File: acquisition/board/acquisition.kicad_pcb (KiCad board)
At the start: 4 copper layers, 0 parts

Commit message: Finished footprint assignment
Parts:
- added C1: 0.1 uF, azonenberg_pcb:EIA_0402_CAP_NOSILK, F.Cu at (151.9, 72.8)
- added C10: 0.1 uF, azonenberg_pcb:EIA_0402_CAP_NOSILK, F.Cu at (141.8, 83.6)
- added C100: 0.47 uF, azonenberg_pcb:EIA_0402_CAP_NOSILK, F.Cu at (151.1, 74.3)
- added C101: 0.47 uF, azonenberg_pcb:EIA_0402_CAP_NOSILK, F.Cu at (141.8, 86.6)
- added C102: 0.47 uF, azonenberg_pcb:EIA_0402_CAP_NOSILK, F.Cu at (113.7, 113.7)
- added C103: 0.47 uF, azonenberg_pcb:EIA_0402_CAP_NOSILK, F.Cu at (111.2, 112.2)
- added C104: 0.47 uF, azonenberg_pcb:EIA_0402_CAP_NOSILK, F.Cu at (139.3, 86.8)
- added C105: 0.47 uF, azonenberg_pcb:EIA_0402_CAP_NOSILK, F.Cu at (146.8, 85.1)
- added C106: 0.47 uF, azonenberg_pcb:EIA_0402_CAP_NOSILK, F.Cu at (139.3, 85.3)
- added C107: 0.47 uF, azonenberg_pcb:EIA_0402_CAP_NOSILK, F.Cu at (149.4, 72.8)
- added C108: 4.7 uF, azonenberg_pcb:EIA_0603_CAP_NOSILK, F.Cu at (66.0, 54.9)
- added C109: 4.7 uF, azonenberg_pcb:EIA_0603_CAP_NOSILK, F.Cu at (55.4, 49.4)
- added C11: 0.1 uF, azonenberg_pcb:EIA_0402_CAP_NOSILK, F.Cu at (148.6, 76.1)
- added C110: 4.7 uF, azonenberg_pcb:EIA_0603_CAP_NOSILK, F.Cu at (58.7, 51.2)
- added C111: 4.7 uF, azonenberg_pcb:EIA_0603_CAP_NOSILK, F.Cu at (55.4, 51.2)
- added C112: 0.47 uF, azonenberg_pcb:EIA_0402_CAP_NOSILK, F.Cu at (65.6, 64.0)
- added C113: 0.47 uF, azonenberg_pcb:EIA_0402_CAP_NOSILK, F.Cu at (65.6, 59.5)
- added C114: 0.47 uF, azonenberg_pcb:EIA_0402_CAP_NOSILK, F.Cu at (78.1, 60.7)
- added C115: 0.47 uF, azonenberg_pcb:EIA_0402_CAP_NOSILK, F.Cu at (65.6, 58.0)
- added C116: 0.47 uF, azonenberg_pcb:EIA_0402_CAP_NOSILK, F.Cu at (92.0, 45.6)
- added C117: 0.47 uF, azonenberg_pcb:EIA_0402_CAP_NOSILK, F.Cu at (73.1, 57.7)
- added C118: 0.47 uF, azonenberg_pcb:EIA_0402_CAP_NOSILK, F.Cu at (87.0, 47.1)
- added C119: 0.47 uF, azonenberg_pcb:EIA_0402_CAP_NOSILK, F.Cu at (49.5, 75.9)
- added C12: 0.1 uF, azonenberg_pcb:EIA_0402_CAP_NOSILK, F.Cu at (144.3, 83.6)
- added C120: 0.47 uF, azonenberg_pcb:EIA_0402_CAP_NOSILK, F.Cu at (44.5, 73.5)
- added C121: 0.47 uF, azonenberg_pcb:EIA_0402_CAP_NOSILK, F.Cu at (89.5, 44.1)
- added C122: 0.47 uF, azonenberg_pcb:EIA_0402_CAP_NOSILK, F.Cu at (47.0, 72.0)
- added C123: 0.47 uF, azonenberg_pcb:EIA_0402_CAP_NOSILK, F.Cu at (68.1, 56.5)
- added C124: 0.47 uF, azonenberg_pcb:EIA_0402_CAP_NOSILK, F.Cu at (49.5, 72.9)
- added C125: 0.47 uF, azonenberg_pcb:EIA_0402_CAP_NOSILK, F.Cu at (80.6, 56.2)
- added C126: 0.47 uF, azonenberg_pcb:EIA_0402_CAP_NOSILK, F.Cu at (87.0, 44.1)
- added C127: 0.47 uF, azonenberg_pcb:EIA_0402_CAP_NOSILK, F.Cu at (44.5, 75.0)
- added C128: 4.7 uF, azonenberg_pcb:EIA_0603_CAP_NOSILK, F.Cu at (48.2, 70.3)
- added C129: 4.7 uF, azonenberg_pcb:EIA_0603_CAP_NOSILK, F.Cu at (58.7, 49.4)
- added C13: 0.47 uF, azonenberg_pcb:EIA_0402_CAP_NOSILK, F.Cu at (145.4, 79.1)
- added C130: 4.7 uF, azonenberg_pcb:EIA_0603_CAP_NOSILK, F.Cu at (48.2, 68.5)
- added C131: 4.7 uF, azonenberg_pcb:EIA_0603_CAP_NOSILK, F.Cu at (44.9, 68.5)
- added C132: 0.47 uF, azonenberg_pcb:EIA_0402_CAP_NOSILK, F.Cu at (78.1, 56.2)
- added C133: 0.47 uF, azonenberg_pcb:EIA_0402_CAP_NOSILK, F.Cu at (75.6, 60.7)
- added C134: 0.47 uF, azonenberg_pcb:EIA_0402_CAP_NOSILK, F.Cu at (59.5, 76.0)
- added C135: 0.47 uF, azonenberg_pcb:EIA_0402_CAP_NOSILK, F.Cu at (73.1, 56.2)
- added C136: 0.47 uF, azonenberg_pcb:EIA_0402_CAP_NOSILK, F.Cu at (73.1, 65.2)
- added C137: 0.47 uF, azonenberg_pcb:EIA_0402_CAP_NOSILK, F.Cu at (70.6, 61.0)
- added C138: 0.47 uF, azonenberg_pcb:EIA_0402_CAP_NOSILK, F.Cu at (57.0, 76.0)
- added C139: 0.47 uF, azonenberg_pcb:EIA_0402_CAP_NOSILK, F.Cu at (68.1, 59.5)
- added C14: 4.7 uF, azonenberg_pcb:EIA_0603_CAP_NOSILK, F.Cu at (129.1, 88.8)
- added C140: 0.47 uF, azonenberg_pcb:EIA_0402_CAP_NOSILK, F.Cu at (44.5, 72.0)
- added C141: 0.47 uF, azonenberg_pcb:EIA_0402_CAP_NOSILK, F.Cu at (44.5, 76.5)
- added C142: 0.47 uF, azonenberg_pcb:EIA_0402_CAP_NOSILK, F.Cu at (75.6, 57.7)
- added C143: 0.47 uF, azonenberg_pcb:EIA_0402_CAP_NOSILK, F.Cu at (68.1, 70.0)
- added C144: 0.47 uF, azonenberg_pcb:EIA_0402_CAP_NOSILK, F.Cu at (68.1, 62.5)
- added C145: 0.47 uF, azonenberg_pcb:EIA_0402_CAP_NOSILK, F.Cu at (75.6, 59.2)
- added C146: 0.47 uF, azonenberg_pcb:EIA_0402_CAP_NOSILK, F.Cu at (87.0, 45.6)
- added C147: 0.47 uF, azonenberg_pcb:EIA_0402_CAP_NOSILK, F.Cu at (89.5, 48.6)
- added C148: 0.47 uF, azonenberg_pcb:EIA_0402_CAP_NOSILK, F.Cu at (72.2, 54.7)
- added C149: 0.47 uF, azonenberg_pcb:EIA_0402_CAP_NOSILK, F.Cu at (84.5, 44.1)
- added C15: 0.47 uF, azonenberg_pcb:EIA_0402_CAP_NOSILK, F.Cu at (151.1, 75.8)
- added C150: 0.47 uF, azonenberg_pcb:EIA_0402_CAP_NOSILK, F.Cu at (80.6, 57.7)
- added C151: 0.47 uF, azonenberg_pcb:EIA_0402_CAP_NOSILK, F.Cu at (73.1, 62.2)
- added C152: 0.47 uF, azonenberg_pcb:EIA_0402_CAP_NOSILK, F.Cu at (82.2, 54.7)
- added C153: 0.47 uF, azonenberg_pcb:EIA_0402_CAP_NOSILK, F.Cu at (78.1, 59.2)
- added C154: 0.47 uF, azonenberg_pcb:EIA_0402_CAP_NOSILK, F.Cu at (47.0, 76.5)
- added C155: 0.47 uF, azonenberg_pcb:EIA_0402_CAP_NOSILK, F.Cu at (52.0, 74.4)
- added C156: 0.47 uF, azonenberg_pcb:EIA_0402_CAP_NOSILK, F.Cu at (87.0, 48.6)
- added C157: 0.47 uF, azonenberg_pcb:EIA_0402_CAP_NOSILK, F.Cu at (68.1, 67.0)
- added C158: 0.47 uF, azonenberg_pcb:EIA_0402_CAP_NOSILK, F.Cu at (70.6, 64.0)
- added C159: 0.47 uF, azonenberg_pcb:EIA_0402_CAP_NOSILK, F.Cu at (73.1, 59.2)
- added C16: 0.47 uF, azonenberg_pcb:EIA_0402_CAP_NOSILK, F.Cu at (142.9, 77.6)
- added C160: 0.47 uF, azonenberg_pcb:EIA_0402_CAP_NOSILK, F.Cu at (54.5, 76.0)
- added C161: 0.47 uF, azonenberg_pcb:EIA_0402_CAP_NOSILK, F.Cu at (89.5, 47.1)
- added C162: 0.47 uF, azonenberg_pcb:EIA_0402_CAP_NOSILK, F.Cu at (84.5, 48.6)
- added C163: 0.47 uF, azonenberg_pcb:EIA_0402_CAP_NOSILK, F.Cu at (89.5, 45.6)
- added C164: 4.7 uF, azonenberg_pcb:EIA_0603_CAP_NOSILK, F.Cu at (110.9, 105.4)
- added C165: 0.1 uF, azonenberg_pcb:EIA_0402_CAP_NOSILK, F.Cu at (111.0, 118.2)
- added C166: 10 nF, azonenberg_pcb:EIA_0603_CAP_NOSILK, F.Cu at (110.9, 103.6)
- added C167: 0.47 uF, azonenberg_pcb:EIA_0402_CAP_NOSILK, F.Cu at (99.1, 119.7)
- added C168: 0.47 uF, azonenberg_pcb:EIA_0402_CAP_NOSILK, F.Cu at (107.9, 115.2)
- added C169: 10 nF, azonenberg_pcb:EIA_0603_CAP_NOSILK, F.Cu at (114.2, 105.4)
- added C17: 0.47 uF, azonenberg_pcb:EIA_0402_CAP_NOSILK, F.Cu at (153.6, 75.8)
- added C170: 4.7 uF, azonenberg_pcb:EIA_0603_CAP_NOSILK, F.Cu at (100.0, 118.0)
- added C171: 4.7 uF, azonenberg_pcb:EIA_0603_CAP_NOSILK, F.Cu at (110.9, 107.2)
- added C172: 0.47 uF, azonenberg_pcb:EIA_0402_CAP_NOSILK, F.Cu at (110.4, 115.2)
- added C173: 0.47 uF, azonenberg_pcb:EIA_0402_CAP_NOSILK, F.Cu at (117.1, 103.5)
- added C174: 0.47 uF, azonenberg_pcb:EIA_0402_CAP_NOSILK, F.Cu at (106.0, 117.8)
- added C175: 0.47 uF, azonenberg_pcb:EIA_0402_CAP_NOSILK, F.Cu at (116.3, 107.0)
- added C176: 0.47 uF, azonenberg_pcb:EIA_0402_CAP_NOSILK, F.Cu at (108.5, 119.8)
- added C177: 0.47 uF, azonenberg_pcb:EIA_0402_CAP_NOSILK, F.Cu at (113.8, 108.5)
- added C178: 0.1 uF, azonenberg_pcb:EIA_0402_CAP_NOSILK, F.Cu at (108.5, 116.8)
- added C179: 0.47 uF, azonenberg_pcb:EIA_0402_CAP_NOSILK, F.Cu at (111.2, 113.7)
- added C18: 0.47 uF, azonenberg_pcb:EIA_0402_CAP_NOSILK, F.Cu at (148.6, 74.6)
- added C180: 4.7 uF, azonenberg_pcb:EIA_0603_CAP_NOSILK, F.Cu at (171.0, 49.4)
- added C181: 0.47 uF, azonenberg_pcb:EIA_0402_CAP_NOSILK, F.Cu at (161.9, 60.0)
- added C182: 0.1 uF, azonenberg_pcb:EIA_0402_CAP_NOSILK, F.Cu at (171.5, 52.5)
- added C183: 0.47 uF, azonenberg_pcb:EIA_0402_CAP_NOSILK, F.Cu at (166.5, 52.5)
- added C184: 0.47 uF, azonenberg_pcb:EIA_0402_CAP_NOSILK, F.Cu at (165.6, 58.5)
- added C185: 0.47 uF, azonenberg_pcb:EIA_0402_CAP_NOSILK, F.Cu at (166.9, 55.5)
- added C186: 0.47 uF, azonenberg_pcb:EIA_0402_CAP_NOSILK, F.Cu at (165.6, 57.0)
- added C187: 0.47 uF, azonenberg_pcb:EIA_0402_CAP_NOSILK, F.Cu at (173.9, 49.2)
- added C188: 0.47 uF, azonenberg_pcb:EIA_0402_CAP_NOSILK, F.Cu at (169.0, 52.5)
- added C189: 0.1 uF, azonenberg_pcb:EIA_0402_CAP_NOSILK, F.Cu at (65.6, 68.5)
- added C19: 4.7 uF, azonenberg_pcb:EIA_0603_CAP_NOSILK, F.Cu at (146.5, 73.0)
- added C190: 0.1 uF, azonenberg_pcb:EIA_0402_CAP_NOSILK, F.Cu at (68.1, 58.0)
- added C191: 0.1 uF, azonenberg_pcb:EIA_0402_CAP_NOSILK, F.Cu at (74.7, 54.7)
- added C192: 0.1 uF, azonenberg_pcb:EIA_0402_CAP_NOSILK, F.Cu at (52.0, 76.0)
- added C193: 10 uF, azonenberg_pcb:EIA_1206_CAP_NOSILK, F.Cu at (75.9, 81.9)
- added C194: 47 uF, azonenberg_pcb:EIA_1206_CAP_NOSILK, F.Cu at (75.9, 84.5)
- added C195: 47 uF, azonenberg_pcb:EIA_1206_CAP_NOSILK, F.Cu at (51.8, 93.5)
- added C196: 47 uF, azonenberg_pcb:EIA_1206_CAP_NOSILK, F.Cu at (55.5, 104.0)
- added C197: 47 uF, azonenberg_pcb:EIA_1206_CAP_NOSILK, F.Cu at (55.5, 101.4)
- added C198: 22 uF, azonenberg_pcb:EIA_1210_CAP_NOSILK, F.Cu at (70.2, 87.9)
- added C199: 22 uF, azonenberg_pcb:EIA_1210_CAP_NOSILK, F.Cu at (75.2, 87.9)
- added C2: 0.1 uF, azonenberg_pcb:EIA_0402_CAP_NOSILK, F.Cu at (147.6, 82.1)
- added C20: 0.47 uF, azonenberg_pcb:EIA_0402_CAP_NOSILK, F.Cu at (150.1, 80.6)
- added C200: 22 uF, azonenberg_pcb:EIA_1210_CAP_NOSILK, F.Cu at (61.2, 97.7)
- added C201: 22 uF, azonenberg_pcb:EIA_1210_CAP_NOSILK, F.Cu at (68.6, 92.3)
- added C202: 1 uF, azonenberg_pcb:EIA_0603_CAP_NOSILK, F.Cu at (69.3, 54.9)
- added C203: 1 uF, azonenberg_pcb:EIA_0603_CAP_NOSILK, F.Cu at (55.4, 53.0)
- added C204: 1 uF, azonenberg_pcb:EIA_0603_CAP_NOSILK, F.Cu at (58.7, 53.0)
- added C205: 1 uF, azonenberg_pcb:EIA_0603_CAP_NOSILK, F.Cu at (44.9, 70.3)
- added C206: 0.1 uF, azonenberg_pcb:EIA_0402_CAP_NOSILK, F.Cu at (79.7, 54.7)
- added C207: 0.1 uF, azonenberg_pcb:EIA_0402_CAP_NOSILK, F.Cu at (70.6, 58.0)
- added C208: 0.1 uF, azonenberg_pcb:EIA_0402_CAP_NOSILK, F.Cu at (62.0, 76.0)
- added C209: 0.1 uF, azonenberg_pcb:EIA_0402_CAP_NOSILK, F.Cu at (78.1, 57.7)
- added C21: 0.47 uF, azonenberg_pcb:EIA_0402_CAP_NOSILK, F.Cu at (139.4, 88.3)
- added C210: DNP, azonenberg_pcb:EIA_0402_CAP_NOSILK, F.Cu at (85.7, 82.8)
- added C211: DNP, azonenberg_pcb:EIA_0402_CAP_NOSILK, F.Cu at (83.2, 82.8)
- added C212: DNP, azonenberg_pcb:EIA_0402_CAP_NOSILK, F.Cu at (61.7, 105.2)
- added C213: DNP, azonenberg_pcb:EIA_0402_CAP_NOSILK, F.Cu at (68.2, 95.0)
- added C214: 4.7 uF, azonenberg_pcb:EIA_0603_CAP_NOSILK, F.Cu at (65.3, 96.6)
- added C215: 4.7 uF, azonenberg_pcb:EIA_0603_CAP_NOSILK, F.Cu at (65.3, 98.4)
- added C216: DNP, azonenberg_pcb:EIA_0402_CAP_NOSILK, F.Cu at (75.7, 90.6)
- added C217: DNP, azonenberg_pcb:EIA_0402_CAP_NOSILK, F.Cu at (70.7, 96.5)
- added C218: 4.7 uF, azonenberg_pcb:EIA_0603_CAP_NOSILK, F.Cu at (79.4, 86.7)
- added C219: 4.7 uF, azonenberg_pcb:EIA_0603_CAP_NOSILK, F.Cu at (72.8, 90.8)
- added C22: 0.47 uF, azonenberg_pcb:EIA_0402_CAP_NOSILK, F.Cu at (141.8, 85.1)
- added C220: 4.7 uF, azonenberg_pcb:EIA_0603_CAP_NOSILK, F.Cu at (110.9, 109.0)
- added C221: 4.7 uF, azonenberg_pcb:EIA_0603_CAP_NOSILK, F.Cu at (65.3, 100.2)
- added C222: 4.7 uF, azonenberg_pcb:EIA_0603_CAP_NOSILK, F.Cu at (72.8, 92.5)
- added C23: 0.47 uF, azonenberg_pcb:EIA_0402_CAP_NOSILK, F.Cu at (139.3, 82.3)
- added C24: 0.47 uF, azonenberg_pcb:EIA_0402_CAP_NOSILK, F.Cu at (131.9, 88.6)
- added C25: 0.47 uF, azonenberg_pcb:EIA_0402_CAP_NOSILK, F.Cu at (147.9, 77.6)
- added C26: 0.47 uF, azonenberg_pcb:EIA_0402_CAP_NOSILK, F.Cu at (153.6, 74.3)
- added C27: 0.47 uF, azonenberg_pcb:EIA_0402_CAP_NOSILK, F.Cu at (152.9, 77.3)
- added C28: 0.47 uF, azonenberg_pcb:EIA_0402_CAP_NOSILK, F.Cu at (139.3, 83.8)
- added C29: 10 uF, azonenberg_pcb:EIA_0805_CAP_NOSILK, F.Cu at (139.8, 78.5)
- added C3: 0.1 uF, azonenberg_pcb:EIA_0402_CAP_NOSILK, F.Cu at (145.1, 80.6)
- added C30: 47 pF, azonenberg_pcb:EIA_0402_CAP_NOSILK, F.Cu at (136.9, 88.6)
- added C31: 3900 pF, azonenberg_pcb:EIA_0402_CAP_NOSILK, F.Cu at (150.4, 77.6)
- added C32: 0.1 uF, azonenberg_pcb:EIA_0402_CAP_NOSILK, F.Cu at (142.6, 82.1)
- added C33: 4.7 uF, azonenberg_pcb:EIA_0603_CAP_NOSILK, F.Cu at (113.7, 84.1)
- added C34: 4.7 uF, azonenberg_pcb:EIA_0603_CAP_NOSILK, F.Cu at (95.4, 95.3)
- added C35: 4.7 uF, azonenberg_pcb:EIA_0603_CAP_NOSILK, F.Cu at (102.1, 88.8)
- added C36: 0.47 uF, azonenberg_pcb:EIA_0402_CAP_NOSILK, F.Cu at (109.1, 95.0)
- added C37: 0.47 uF, azonenberg_pcb:EIA_0402_CAP_NOSILK, F.Cu at (106.6, 93.8)
- added C38: 0.47 uF, azonenberg_pcb:EIA_0402_CAP_NOSILK, F.Cu at (108.3, 90.5)
- added C39: 0.47 uF, azonenberg_pcb:EIA_0402_CAP_NOSILK, F.Cu at (103.3, 92.2)
- added C4: 0.1 uF, azonenberg_pcb:EIA_0402_CAP_NOSILK, F.Cu at (152.9, 78.8)
- added C40: 0.47 uF, azonenberg_pcb:EIA_0402_CAP_NOSILK, F.Cu at (101.6, 95.8)
- added C41: 330 uF, azonenberg_pcb:EIA_1210_CAP_NOSILK, F.Cu at (92.9, 92.4)
- added C42: 100 uF, azonenberg_pcb:EIA_1206_CAP_NOSILK, F.Cu at (92.9, 89.2)
- added C43: 0.47 uF, azonenberg_pcb:EIA_0402_CAP_NOSILK, F.Cu at (104.1, 96.8)
- added C44: 0.47 uF, azonenberg_pcb:EIA_0402_CAP_NOSILK, F.Cu at (110.8, 90.5)
- added C45: 4.7 uF, azonenberg_pcb:EIA_0603_CAP_NOSILK, F.Cu at (100.4, 92.7)
- added C46: 100 uF, azonenberg_pcb:EIA_1206_CAP_NOSILK, F.Cu at (111.2, 81.9)
- added C47: 0.47 uF, azonenberg_pcb:EIA_0402_CAP_NOSILK, F.Cu at (114.1, 88.8)
- added C48: 0.47 uF, azonenberg_pcb:EIA_0402_CAP_NOSILK, F.Cu at (106.6, 96.8)
- added C49: 4.7 uF, azonenberg_pcb:EIA_0603_CAP_NOSILK, F.Cu at (105.4, 90.6)
- added C5: 0.1 uF, azonenberg_pcb:EIA_0402_CAP_NOSILK, F.Cu at (134.4, 88.6)
- added C50: 47 uF, azonenberg_pcb:EIA_1210_CAP_NOSILK, F.Cu at (97.9, 89.8)
- added C51: 0.47 uF, azonenberg_pcb:EIA_0402_CAP_NOSILK, F.Cu at (91.7, 98.8)
- added C52: 0.47 uF, azonenberg_pcb:EIA_0402_CAP_NOSILK, F.Cu at (111.6, 92.0)
- added C53: 4.7 uF, azonenberg_pcb:EIA_0603_CAP_NOSILK, F.Cu at (97.1, 92.7)
- added C54: 4.7 uF, azonenberg_pcb:EIA_0603_CAP_NOSILK, F.Cu at (92.1, 95.3)
- added C55: 0.47 uF, azonenberg_pcb:EIA_0402_CAP_NOSILK, F.Cu at (118.3, 81.3)
- added C56: 0.47 uF, azonenberg_pcb:EIA_0402_CAP_NOSILK, F.Cu at (106.6, 98.2)
- added C57: 0.47 uF, azonenberg_pcb:EIA_0402_CAP_NOSILK, F.Cu at (119.1, 84.3)
- added C58: 4.7 uF, azonenberg_pcb:EIA_0603_CAP_NOSILK, F.Cu at (98.7, 98.1)
- added C59: 0.47 uF, azonenberg_pcb:EIA_0402_CAP_NOSILK, F.Cu at (109.1, 93.5)
- added C6: 0.1 uF, azonenberg_pcb:EIA_0402_CAP_NOSILK, F.Cu at (141.9, 88.1)
- added C60: 0.47 uF, azonenberg_pcb:EIA_0402_CAP_NOSILK, F.Cu at (120.8, 81.3)
- added C61: 0.47 uF, azonenberg_pcb:EIA_0402_CAP_NOSILK, F.Cu at (121.6, 82.8)
- added C62: 4.7 uF, azonenberg_pcb:EIA_0603_CAP_NOSILK, F.Cu at (95.4, 97.1)
- added C63: 0.47 uF, azonenberg_pcb:EIA_0402_CAP_NOSILK, F.Cu at (111.6, 89.0)
- added C64: 0.47 uF, azonenberg_pcb:EIA_0402_CAP_NOSILK, F.Cu at (108.3, 92.0)
- added C65: 0.47 uF, azonenberg_pcb:EIA_0402_CAP_NOSILK, F.Cu at (111.6, 87.5)
- added C66: 4.7 uF, azonenberg_pcb:EIA_0603_CAP_NOSILK, F.Cu at (98.7, 94.5)
- added C67: 0.47 uF, azonenberg_pcb:EIA_0402_CAP_NOSILK, F.Cu at (114.1, 90.2)
- added C68: 0.47 uF, azonenberg_pcb:EIA_0402_CAP_NOSILK, F.Cu at (116.6, 83.2)
- added C69: 4.7 uF, azonenberg_pcb:EIA_0603_CAP_NOSILK, F.Cu at (92.1, 97.1)
- added C7: 0.1 uF, azonenberg_pcb:EIA_0402_CAP_NOSILK, F.Cu at (144.3, 85.1)
- added C70: 0.47 uF, azonenberg_pcb:EIA_0402_CAP_NOSILK, F.Cu at (104.1, 98.2)
- added C71: 0.47 uF, azonenberg_pcb:EIA_0402_CAP_NOSILK, F.Cu at (106.6, 95.2)
- added C72: 4.7 uF, azonenberg_pcb:EIA_0603_CAP_NOSILK, F.Cu at (110.4, 84.1)
- added C73: 0.47 uF, azonenberg_pcb:EIA_0402_CAP_NOSILK, F.Cu at (104.1, 93.8)
- added C74: 0.47 uF, azonenberg_pcb:EIA_0402_CAP_NOSILK, F.Cu at (94.2, 98.8)
- added C75: 4.7 uF, azonenberg_pcb:EIA_0603_CAP_NOSILK, F.Cu at (110.4, 85.9)
- added C76: 0.47 uF, azonenberg_pcb:EIA_0402_CAP_NOSILK, F.Cu at (105.8, 92.2)
- added C77: 4.7 uF, azonenberg_pcb:EIA_0603_CAP_NOSILK, F.Cu at (102.1, 90.6)
- added C78: 0.47 uF, azonenberg_pcb:EIA_0402_CAP_NOSILK, F.Cu at (119.1, 82.8)
- added C79: 4.7 uF, azonenberg_pcb:EIA_0603_CAP_NOSILK, F.Cu at (105.4, 88.8)
- added C8: 0.1 uF, azonenberg_pcb:EIA_0402_CAP_NOSILK, F.Cu at (146.8, 83.6)
- added C80: 0.47 uF, azonenberg_pcb:EIA_0402_CAP_NOSILK, F.Cu at (116.6, 86.2)
- added C81: 4.7 uF, azonenberg_pcb:EIA_0603_CAP_NOSILK, F.Cu at (115.4, 81.5)
- added C82: 0.47 uF, azonenberg_pcb:EIA_0402_CAP_NOSILK, F.Cu at (116.6, 84.7)
- added C83: 4.7 uF, azonenberg_pcb:EIA_0603_CAP_NOSILK, F.Cu at (129.1, 104.2)
- added C84: 0.47 uF, azonenberg_pcb:EIA_0402_CAP_NOSILK, F.Cu at (136.8, 97.0)
- added C85: 0.47 uF, azonenberg_pcb:EIA_0402_CAP_NOSILK, F.Cu at (136.8, 94.0)
- added C86: 0.47 uF, azonenberg_pcb:EIA_0402_CAP_NOSILK, F.Cu at (136.8, 98.5)
- added C87: 4.7 uF, azonenberg_pcb:EIA_0603_CAP_NOSILK, F.Cu at (167.8, 65.9)
- added C88: 0.47 uF, azonenberg_pcb:EIA_0402_CAP_NOSILK, F.Cu at (169.9, 67.5)
- added C89: 4.7 uF, azonenberg_pcb:EIA_0603_CAP_NOSILK, F.Cu at (159.7, 76.0)
- added C9: 0.1 uF, azonenberg_pcb:EIA_0402_CAP_NOSILK, F.Cu at (142.9, 79.1)
- added C90: 0.47 uF, azonenberg_pcb:EIA_0402_CAP_NOSILK, F.Cu at (159.3, 77.7)
- added C91: 4.7 uF, azonenberg_pcb:EIA_0603_CAP_NOSILK, F.Cu at (108.7, 88.8)
- added C92: 0.47 uF, azonenberg_pcb:EIA_0402_CAP_NOSILK, F.Cu at (101.6, 97.3)
- added C93: 0.47 uF, azonenberg_pcb:EIA_0402_CAP_NOSILK, F.Cu at (114.1, 87.2)
- added C94: 0.47 uF, azonenberg_pcb:EIA_0402_CAP_NOSILK, F.Cu at (146.1, 74.6)
- added C95: 0.47 uF, azonenberg_pcb:EIA_0402_CAP_NOSILK, F.Cu at (147.6, 80.6)
- added C96: 0.47 uF, azonenberg_pcb:EIA_0402_CAP_NOSILK, F.Cu at (145.1, 82.1)
- added C97: 0.47 uF, azonenberg_pcb:EIA_0402_CAP_NOSILK, F.Cu at (145.4, 77.6)
- added C98: 0.47 uF, azonenberg_pcb:EIA_0402_CAP_NOSILK, F.Cu at (146.1, 76.1)
- added C99: 0.47 uF, azonenberg_pcb:EIA_0402_CAP_NOSILK, F.Cu at (150.4, 79.1)
- added D1: EAST1616RGBA4, azonenberg_pcb:LED_EVERLIGHT_EAST1616RGBA4, F.Cu at (103.2, 118.5)
- added D10: TPD1E05U06QDPYRQ1, azonenberg_pcb:DFN_2_1x0.6_TI_DPY, F.Cu at (131.4, 53.8)
- added D11: TPD1E05U06QDPYRQ1, azonenberg_pcb:DFN_2_1x0.6_TI_DPY, F.Cu at (125.5, 60.2)
- added D12: TPD1E05U06QDPYRQ1, azonenberg_pcb:DFN_2_1x0.6_TI_DPY, F.Cu at (141.0, 45.7)
- added D13: TPD1E05U06QDPYRQ1, azonenberg_pcb:DFN_2_1x0.6_TI_DPY, F.Cu at (141.0, 44.1)
- added D14: TPD1E05U06QDPYRQ1, azonenberg_pcb:DFN_2_1x0.6_TI_DPY, F.Cu at (133.6, 53.8)
- added D15: TPD1E05U06QDPYRQ1, azonenberg_pcb:DFN_2_1x0.6_TI_DPY, F.Cu at (123.3, 63.5)
- added D16: TPD1E05U06QDPYRQ1, azonenberg_pcb:DFN_2_1x0.6_TI_DPY, F.Cu at (123.3, 61.9)
- added D17: TPD1E05U06QDPYRQ1, azonenberg_pcb:DFN_2_1x0.6_TI_DPY, F.Cu at (129.2, 57.0)
- added D18: TPD1E05U06QDPYRQ1, azonenberg_pcb:DFN_2_1x0.6_TI_DPY, F.Cu at (143.2, 44.1)
- added D19: TPD1E05U06QDPYRQ1, azonenberg_pcb:DFN_2_1x0.6_TI_DPY, F.Cu at (133.6, 52.2)
- added D2: GREEN, azonenberg_pcb:EIA_0603_LED, F.Cu at (96.7, 114.7)
- added D20: GREEN, azonenberg_pcb:EIA_0603_LED, F.Cu at (167.7, 49.6)
- added D21: GREEN, azonenberg_pcb:EIA_0603_LED, F.Cu at (159.9, 54.8)
- added D22: GREEN, azonenberg_pcb:EIA_0603_LED, F.Cu at (156.5, 58.5)
- added D23: GREEN, azonenberg_pcb:EIA_0603_LED, F.Cu at (164.0, 54.8)
- added D24: GREEN, azonenberg_pcb:EIA_0603_LED, F.Cu at (160.2, 57.1)
- added D25: TPD1E05U06QDPYRQ1, azonenberg_pcb:DFN_2_1x0.6_TI_DPY, F.Cu at (113.5, 119.0)
- added D26: TPD1E05U06QDPYRQ1, azonenberg_pcb:DFN_2_1x0.6_TI_DPY, F.Cu at (113.5, 117.4)
- added D27: TPD1E05U06QDPYRQ1, azonenberg_pcb:DFN_2_1x0.6_TI_DPY, F.Cu at (111.0, 119.8)
- added D3: GREEN, azonenberg_pcb:EIA_0603_LED, F.Cu at (96.7, 117.0)
- added D4: TPD1E05U06QDPYRQ1, azonenberg_pcb:DFN_2_1x0.6_TI_DPY, F.Cu at (129.2, 55.4)
- added D5: TPD1E05U06QDPYRQ1, azonenberg_pcb:DFN_2_1x0.6_TI_DPY, F.Cu at (129.2, 52.2)
- added D6: TPD1E05U06QDPYRQ1, azonenberg_pcb:DFN_2_1x0.6_TI_DPY, F.Cu at (131.4, 55.4)
- added D7: TPD1E05U06QDPYRQ1, azonenberg_pcb:DFN_2_1x0.6_TI_DPY, F.Cu at (131.4, 52.2)
- added D8: TPD1E05U06QDPYRQ1, azonenberg_pcb:DFN_2_1x0.6_TI_DPY, F.Cu at (129.2, 53.8)
- added D9: TPD1E05U06QDPYRQ1, azonenberg_pcb:DFN_2_1x0.6_TI_DPY, F.Cu at (123.3, 60.2)
- added J1: XILINX_JTAG, azonenberg_pcb:XILINX_JTAG_PTH_MOLEX_0878311420, F.Cu at (99.6, 84.2)
- added J10: MMCX, azonenberg_pcb:CONN_MMCX_J_P_H_ST_EM1, F.Cu at (136.9, 50.6)
- added J11: MMCX, azonenberg_pcb:CONN_MMCX_J_P_H_ST_EM1, F.Cu at (119.2, 50.6)
- added J12: MMCX, azonenberg_pcb:CONN_MMCX_J_P_H_ST_EM1, F.Cu at (125.1, 50.6)
- added J13: MMCX, azonenberg_pcb:CONN_MMCX_J_P_H_ST_EM1, F.Cu at (107.4, 58.7)
- added J14: MMCX, azonenberg_pcb:CONN_MMCX_J_P_H_ST_EM1, F.Cu at (101.5, 58.7)
- added J15: MMCX, azonenberg_pcb:CONN_MMCX_J_P_H_ST_EM1, F.Cu at (113.3, 50.6)
- added J16: MMCX, azonenberg_pcb:CONN_MMCX_J_P_H_ST_EM1, F.Cu at (119.2, 58.7)
- added J17: MMCX, azonenberg_pcb:CONN_MMCX_J_P_H_ST_EM1, F.Cu at (125.1, 58.7)
- added J18: UX60SX-MB-5ST, azonenberg_pcb:CONN_HIROSE_UX60S-MB-5ST_MINI_USB, F.Cu at (107.3, 107.7)
- added J19: CONN_01X05, azonenberg_pcb:CONN_HEADER_2.54MM_1x5, F.Cu at (154.6, 51.0)
- added J2: MMCX, azonenberg_pcb:CONN_MMCX_J_P_H_ST_EM1, F.Cu at (101.5, 66.8)
- added J20: CONN_01X06, azonenberg_pcb:CONN_HEADER_2.54MM_1x6, F.Cu at (155.9, 45.9)
- added J3: MMCX, azonenberg_pcb:CONN_MMCX_J_P_H_ST_EM1, F.Cu at (113.3, 66.8)
- added J4: MMCX, azonenberg_pcb:CONN_MMCX_J_P_H_ST_EM1, F.Cu at (119.2, 66.8)
- added J5: MMCX, azonenberg_pcb:CONN_MMCX_J_P_H_ST_EM1, F.Cu at (107.4, 66.8)
- added J6: MMCX, azonenberg_pcb:CONN_MMCX_J_P_H_ST_EM1, F.Cu at (113.3, 58.7)
- added J7: MMCX, azonenberg_pcb:CONN_MMCX_J_P_H_ST_EM1, F.Cu at (107.4, 50.6)
- added J8: MMCX, azonenberg_pcb:CONN_MMCX_J_P_H_ST_EM1, F.Cu at (101.5, 50.6)
- added J9: MMCX, azonenberg_pcb:CONN_MMCX_J_P_H_ST_EM1, F.Cu at (131.0, 50.6)
- added L1: FERRITE, azonenberg_pcb:EIA_0603_INDUCTOR_NOSILK, F.Cu at (139.7, 80.7)
- added L2: FERRITE, azonenberg_pcb:EIA_0603_INDUCTOR_NOSILK, F.Cu at (98.7, 96.3)
- added L3: FERRITE, azonenberg_pcb:EIA_0603_INDUCTOR_NOSILK, F.Cu at (108.3, 113.6)
- added L4: FERRITE, azonenberg_pcb:EIA_0603_INDUCTOR_NOSILK, F.Cu at (96.2, 119.1)
- added L5: FERRITE, azonenberg_pcb:EIA_0603_INDUCTOR_NOSILK, F.Cu at (114.2, 103.6)
- added L6: NRS5030T2R2NMGJ, azonenberg_pcb:INDUCTOR_YUDEN_NRS5030, F.Cu at (52.9, 84.2)
- added L7: NRS5030T2R2NMGJ, azonenberg_pcb:INDUCTOR_YUDEN_NRS5030, F.Cu at (45.8, 91.3)
- added L8: NRS5030T2R2NMGJ, azonenberg_pcb:INDUCTOR_YUDEN_NRS5030, F.Cu at (45.8, 84.2)
- added L9: NRS5030T2R2NMGJ, azonenberg_pcb:INDUCTOR_YUDEN_NRS5030, F.Cu at (38.2, 102.3)
- added Q1: SSM6N58NU, azonenberg_pcb:DFN_6_0.65MM_2x2MM_GDS, F.Cu at (156.1, 55.5)
- added Q2: SSM6N58NU, azonenberg_pcb:DFN_6_0.65MM_2x2MM_GDS, F.Cu at (163.6, 50.3)
- added R1: 33, azonenberg_pcb:EIA_0402_RES_NOSILK, F.Cu at (70.6, 56.5)
- added R10: 470, azonenberg_pcb:EIA_0402_RES_NOSILK, F.Cu at (147.9, 79.1)
- added R11: 10k, azonenberg_pcb:EIA_0402_RES_NOSILK, F.Cu at (70.6, 59.5)
- added R12: 10k, azonenberg_pcb:EIA_0402_RES_NOSILK, F.Cu at (84.5, 51.6)
- added R13: 33, azonenberg_pcb:EIA_0402_RES_NOSILK, F.Cu at (139.2, 94.0)
- added R14: 33, azonenberg_pcb:EIA_0402_RES_NOSILK, F.Cu at (131.9, 104.0)
- added R15: 33, azonenberg_pcb:EIA_0402_RES_NOSILK, F.Cu at (139.2, 98.5)
- added R16: 33, azonenberg_pcb:EIA_0402_RES_NOSILK, F.Cu at (136.8, 95.5)
- added R17: 33, azonenberg_pcb:EIA_0402_RES_NOSILK, F.Cu at (139.2, 95.5)
- added R18: 33, azonenberg_pcb:EIA_0402_RES_NOSILK, F.Cu at (139.2, 97.0)
- added R19: 33, azonenberg_pcb:EIA_0402_RES_NOSILK, F.Cu at (128.7, 105.8)
- added R2: 33, azonenberg_pcb:EIA_0402_RES_NOSILK, F.Cu at (101.6, 98.8)
- added R20: 33, azonenberg_pcb:EIA_0402_RES_NOSILK, F.Cu at (136.8, 100.0)
- added R21: 33, azonenberg_pcb:EIA_0402_RES_NOSILK, F.Cu at (141.8, 94.0)
- added R22: 10K, azonenberg_pcb:EIA_0402_RES_NOSILK, F.Cu at (112.9, 115.2)
- added R23: 33, azonenberg_pcb:EIA_0402_RES_NOSILK, F.Cu at (106.0, 119.3)
- added R24: 12K, azonenberg_pcb:EIA_0402_RES_NOSILK, F.Cu at (111.0, 116.8)
- added R25: 39K, azonenberg_pcb:EIA_0402_RES_NOSILK, F.Cu at (116.2, 111.5)
- added R26: 470, azonenberg_pcb:EIA_0402_RES_NOSILK, F.Cu at (108.5, 118.2)
- added R27: 470, azonenberg_pcb:EIA_0402_RES_NOSILK, F.Cu at (113.8, 107.0)
- added R28: 2k, azonenberg_pcb:EIA_0402_RES_NOSILK, F.Cu at (110.5, 110.7)
- added R29: 10k, azonenberg_pcb:EIA_0402_RES_NOSILK, F.Cu at (113.7, 112.2)
- added R3: 33, azonenberg_pcb:EIA_0402_RES_NOSILK, F.Cu at (101.6, 94.3)
- added R30: 10k, azonenberg_pcb:EIA_0402_RES_NOSILK, F.Cu at (116.2, 113.0)
- added R31: 0, azonenberg_pcb:EIA_0402_RES_NOSILK, F.Cu at (166.9, 54.0)
- added R32: DNP, azonenberg_pcb:EIA_0402_RES_NOSILK, F.Cu at (169.4, 54.0)
- added R33: 470, azonenberg_pcb:EIA_0402_RES_NOSILK, F.Cu at (159.4, 60.0)
- added R34: 100, azonenberg_pcb:EIA_0402_RES_NOSILK, F.Cu at (128.7, 107.3)
- added R35: 100, azonenberg_pcb:EIA_0402_RES_NOSILK, F.Cu at (134.4, 104.0)
- added R36: 10K, azonenberg_pcb:EIA_0402_RES_NOSILK, F.Cu at (141.8, 95.5)
- added R37: 10K, azonenberg_pcb:EIA_0402_RES_NOSILK, F.Cu at (131.2, 105.8)
- added R38: 33, azonenberg_pcb:EIA_0402_RES_NOSILK, F.Cu at (65.6, 65.5)
- added R39: 10K, azonenberg_pcb:EIA_0402_RES_NOSILK, F.Cu at (52.0, 72.9)
- added R4: 33, azonenberg_pcb:EIA_0402_RES_NOSILK, F.Cu at (167.4, 70.5)
- added R40: 33, azonenberg_pcb:EIA_0402_RES_NOSILK, F.Cu at (70.6, 67.0)
- added R41: 10K, azonenberg_pcb:EIA_0402_RES_NOSILK, F.Cu at (51.1, 69.9)
- added R42: 33, azonenberg_pcb:EIA_0402_RES_NOSILK, F.Cu at (73.1, 60.7)
- added R43: 10K, azonenberg_pcb:EIA_0402_RES_NOSILK, F.Cu at (70.6, 65.5)
- added R44: 33, azonenberg_pcb:EIA_0402_RES_NOSILK, F.Cu at (92.0, 44.1)
- added R45: 10K, azonenberg_pcb:EIA_0402_RES_NOSILK, F.Cu at (68.1, 65.5)
- added R46: 100, azonenberg_pcb:EIA_0402_RES_NOSILK, F.Cu at (65.6, 67.0)
- added R47: 100, azonenberg_pcb:EIA_0402_RES_NOSILK, F.Cu at (84.5, 45.6)
- added R48: 100, azonenberg_pcb:EIA_0402_RES_NOSILK, F.Cu at (51.1, 68.4)
- added R49: 100, azonenberg_pcb:EIA_0402_RES_NOSILK, F.Cu at (65.6, 61.0)
- added R5: 33, azonenberg_pcb:EIA_0402_RES_NOSILK, F.Cu at (159.3, 79.2)
- added R50: 100, azonenberg_pcb:EIA_0402_RES_NOSILK, F.Cu at (47.0, 75.0)
- added R51: 100, azonenberg_pcb:EIA_0402_RES_NOSILK, F.Cu at (77.2, 54.7)
- added R52: 100, azonenberg_pcb:EIA_0402_RES_NOSILK, F.Cu at (68.1, 64.0)
- added R53: 100, azonenberg_pcb:EIA_0402_RES_NOSILK, F.Cu at (65.6, 62.5)
- added R54: 100, azonenberg_pcb:EIA_0402_RES_NOSILK, F.Cu at (75.6, 56.2)
- added R55: 100, azonenberg_pcb:EIA_0402_RES_NOSILK, F.Cu at (73.1, 63.7)
- added R56: 100, azonenberg_pcb:EIA_0402_RES_NOSILK, F.Cu at (49.5, 74.4)
- added R57: 100, azonenberg_pcb:EIA_0402_RES_NOSILK, F.Cu at (68.1, 61.0)
- added R58: 100, azonenberg_pcb:EIA_0402_RES_NOSILK, F.Cu at (84.5, 47.1)
- added R59: 100, azonenberg_pcb:EIA_0402_RES_NOSILK, F.Cu at (68.1, 68.5)
- added R6: 33, azonenberg_pcb:EIA_0402_RES_NOSILK, F.Cu at (167.4, 69.0)
- added R60: 100, azonenberg_pcb:EIA_0402_RES_NOSILK, F.Cu at (65.6, 70.0)
- added R61: 100, azonenberg_pcb:EIA_0402_RES_NOSILK, F.Cu at (47.0, 73.5)
- added R62: 33, azonenberg_pcb:EIA_0402_RES_NOSILK, F.Cu at (70.6, 62.5)
- added R63: 33, azonenberg_pcb:EIA_0402_RES_NOSILK, F.Cu at (84.5, 53.1)
- added R64: 33, azonenberg_pcb:EIA_0402_RES_NOSILK, F.Cu at (51.1, 71.4)
- added R65: 33, azonenberg_pcb:EIA_0402_RES_NOSILK, F.Cu at (87.0, 50.1)
- added R66: 1K, azonenberg_pcb:EIA_0402_RES_NOSILK, F.Cu at (70.7, 95.0)
- added R67: DNP, azonenberg_pcb:EIA_0402_RES_NOSILK, F.Cu at (68.2, 98.0)
- added R68: 1.02M, azonenberg_pcb:EIA_0402_RES_NOSILK, F.Cu at (59.2, 105.2)
- added R69: 324K, azonenberg_pcb:EIA_0402_RES_NOSILK, F.Cu at (64.6, 101.9)
- added R7: 33, azonenberg_pcb:EIA_0402_RES_NOSILK, F.Cu at (170.7, 65.8)
- added R70: 1.02M, azonenberg_pcb:EIA_0402_RES_NOSILK, F.Cu at (58.7, 106.7)
- added R71: 475K, azonenberg_pcb:EIA_0402_RES_NOSILK, F.Cu at (58.7, 108.2)
- added R72: 806K, azonenberg_pcb:EIA_0402_RES_NOSILK, F.Cu at (83.2, 81.3)
- added R73: 649K, azonenberg_pcb:EIA_0402_RES_NOSILK, F.Cu at (68.2, 96.5)
- added R74: 255K, azonenberg_pcb:EIA_0402_RES_NOSILK, F.Cu at (64.6, 103.4)
- added R75: 1.02M, azonenberg_pcb:EIA_0402_RES_NOSILK, F.Cu at (79.0, 88.3)
- added R76: 10K, azonenberg_pcb:EIA_0402_RES_NOSILK, F.Cu at (61.2, 106.7)
- added R77: 470, azonenberg_pcb:EIA_0402_RES_NOSILK, F.Cu at (70.7, 98.0)
- added R78: 18K, azonenberg_pcb:EIA_0402_RES_NOSILK, F.Cu at (85.7, 81.3)
- added R79: 18K, azonenberg_pcb:EIA_0402_RES_NOSILK, F.Cu at (82.3, 86.0)
- added R8: 100, azonenberg_pcb:EIA_0402_RES_NOSILK, F.Cu at (65.6, 71.5)
- added R80: 10K, azonenberg_pcb:EIA_0402_RES_NOSILK, F.Cu at (162.6, 75.8)
- added R81: 10K, azonenberg_pcb:EIA_0402_RES_NOSILK, F.Cu at (84.5, 50.1)
- added R82: 10K, azonenberg_pcb:EIA_0402_RES_NOSILK, F.Cu at (75.6, 62.2)
- added R83: 10K, azonenberg_pcb:EIA_0402_RES_NOSILK, F.Cu at (65.6, 56.5)
- added R84: 10K, azonenberg_pcb:EIA_0402_RES_NOSILK, F.Cu at (65.6, 73.0)
- added R85: 33, azonenberg_pcb:EIA_0402_RES_NOSILK, F.Cu at (116.3, 108.5)
- added R86: 33, azonenberg_pcb:EIA_0402_RES_NOSILK, F.Cu at (115.5, 110.0)
- added R87: 33, azonenberg_pcb:EIA_0402_RES_NOSILK, F.Cu at (113.0, 110.7)
- added R88: 33, azonenberg_pcb:EIA_0402_RES_NOSILK, F.Cu at (117.1, 105.0)
- added R89: 4.7K, azonenberg_pcb:EIA_0402_RES_NOSILK, F.Cu at (113.3, 85.8)
- added R9: 100, azonenberg_pcb:EIA_0402_RES_NOSILK, F.Cu at (142.6, 80.6)
- added R90: 4.7K, azonenberg_pcb:EIA_0402_RES_NOSILK, F.Cu at (104.1, 95.2)
- added R91: 4.7K, azonenberg_pcb:EIA_0402_RES_NOSILK, F.Cu at (116.6, 87.7)
- added R92: 4.7K, azonenberg_pcb:EIA_0402_RES_NOSILK, F.Cu at (170.6, 51.0)
- added R93: 4.7K, azonenberg_pcb:EIA_0402_RES_NOSILK, F.Cu at (163.1, 57.0)
- added R94: 4.7K, azonenberg_pcb:EIA_0402_RES_NOSILK, F.Cu at (163.1, 58.5)
- added R95: 4.7K, azonenberg_pcb:EIA_0402_RES_NOSILK, F.Cu at (173.1, 51.0)
- added R96: 4.7K, azonenberg_pcb:EIA_0402_RES_NOSILK, F.Cu at (167.4, 67.5)
- added TP1: TESTPOINT, azonenberg_pcb:TESTPOINT_SMT_0.5MM, F.Cu at (143.9, 88.8)
- added TP10: U.FL, azonenberg_pcb:CONN_U.FL_TE_1909763-1, F.Cu at (50.2, 101.9)
- added TP11: U.FL, azonenberg_pcb:CONN_U.FL_TE_1909763-1, F.Cu at (63.4, 93.0)
- added TP12: U.FL, azonenberg_pcb:CONN_U.FL_TE_1909763-1, F.Cu at (50.1, 107.3)
- added TP13: U.FL, azonenberg_pcb:CONN_U.FL_TE_1909763-1, F.Cu at (65.0, 87.6)
- added TP14: U.FL, azonenberg_pcb:CONN_U.FL_TE_1909763-1, F.Cu at (55.9, 97.4)
- added TP15: U.FL, azonenberg_pcb:CONN_U.FL_TE_1909763-1, F.Cu at (70.7, 83.2)
- added TP16: U.FL, azonenberg_pcb:CONN_U.FL_TE_1909763-1, F.Cu at (57.8, 92.0)
- added TP17: KEYSTONE_5016, azonenberg_pcb:TESTPOINT_SMT_KEYSTONE_5016, F.Cu at (65.0, 82.8)
- added TP18: KEYSTONE_5016, azonenberg_pcb:TESTPOINT_SMT_KEYSTONE_5016, F.Cu at (50.3, 97.1)
- added TP19: KEYSTONE_5016, azonenberg_pcb:TESTPOINT_SMT_KEYSTONE_5016, F.Cu at (37.4, 108.1)
- added TP2: TESTPOINT, azonenberg_pcb:TESTPOINT_SMT_0.5MM, F.Cu at (145.4, 88.8)
- added TP20: KEYSTONE_5016, azonenberg_pcb:TESTPOINT_SMT_KEYSTONE_5016, F.Cu at (59.3, 87.2)
- added TP21: KEYSTONE_5016, azonenberg_pcb:TESTPOINT_SMT_KEYSTONE_5016, F.Cu at (44.6, 97.1)
- added TP22: KEYSTONE_5016, azonenberg_pcb:TESTPOINT_SMT_KEYSTONE_5016, F.Cu at (52.2, 90.0)
- added TP23: KEYSTONE_5016, azonenberg_pcb:TESTPOINT_SMT_KEYSTONE_5016, F.Cu at (59.3, 82.8)
- added TP24: KEYSTONE_5016, azonenberg_pcb:TESTPOINT_SMT_KEYSTONE_5016, F.Cu at (44.6, 101.5)
- added TP25: TESTPOINT, azonenberg_pcb:TESTPOINT_SMT_0.5MM, F.Cu at (72.7, 94.2)
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
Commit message: Initial layout floorplanning
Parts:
- moved C193 128.8 mm to (204.4, 91.1)
- moved C194 128.8 mm to (204.4, 93.7)
- moved C198 128.8 mm to (198.7, 97.1)
- moved C199 128.8 mm to (203.7, 97.1)
- moved C200 128.8 mm to (189.7, 106.9)
- moved C201 128.8 mm to (197.1, 101.5)
- moved C210 128.8 mm to (214.2, 92.1)
- moved C211 128.8 mm to (211.7, 92.1)
- moved C213 128.8 mm to (196.7, 104.2)
- moved C216 128.8 mm to (204.2, 99.8)
- moved C217 128.8 mm to (199.2, 105.8)
- moved C218 128.8 mm to (207.9, 95.9)
- moved C219 128.8 mm to (201.3, 100.0)
- moved C222 128.8 mm to (201.3, 101.8)
- moved L6 128.8 mm to (181.4, 93.4)
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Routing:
- net /GND: track 0.00 -> 161.8 mm, vias 0 -> 40
- net /D1V8: track 0.00 -> 117.8 mm, vias 0 -> 30
- net /1V0: track 0.00 -> 43.3 mm, vias 0 -> 9
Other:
- copper layers 4 -> 6

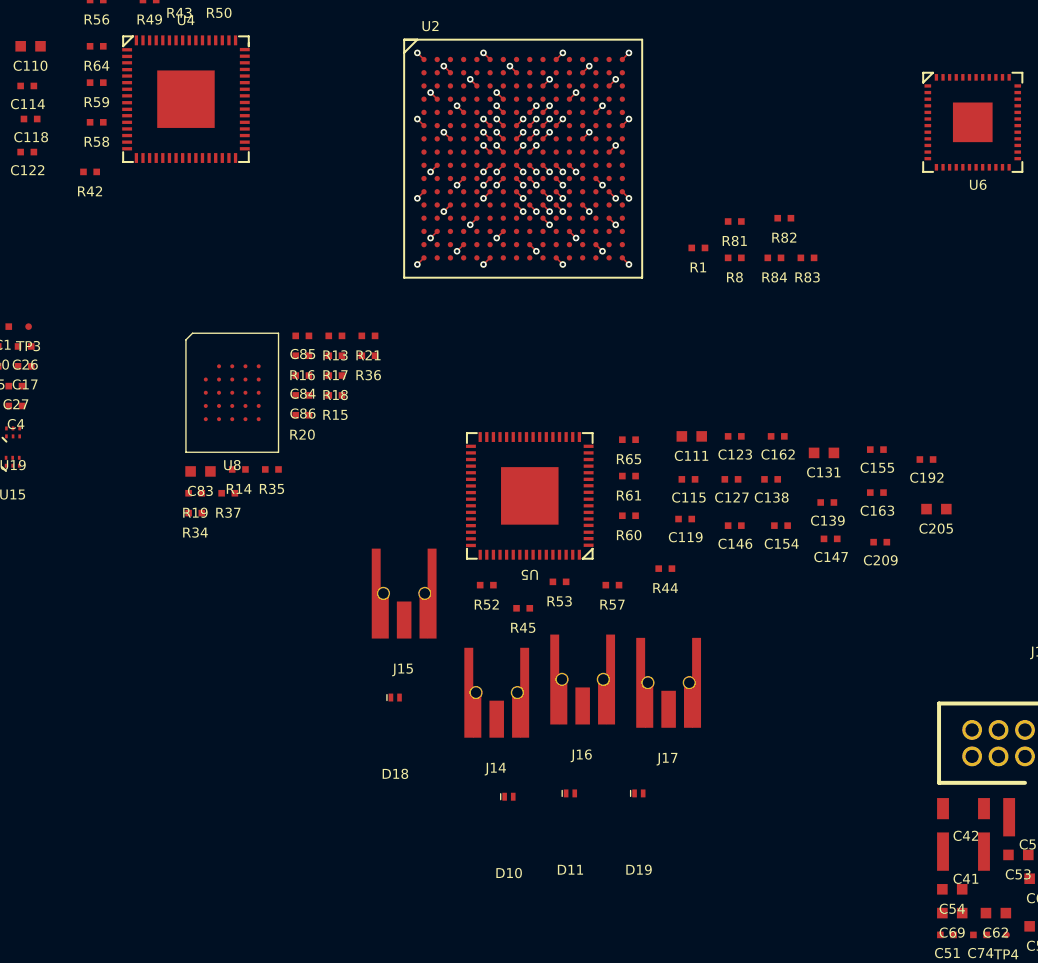
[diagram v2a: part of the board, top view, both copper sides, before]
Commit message: Finished initial routing of RAM, hooked up almost all of first ADC
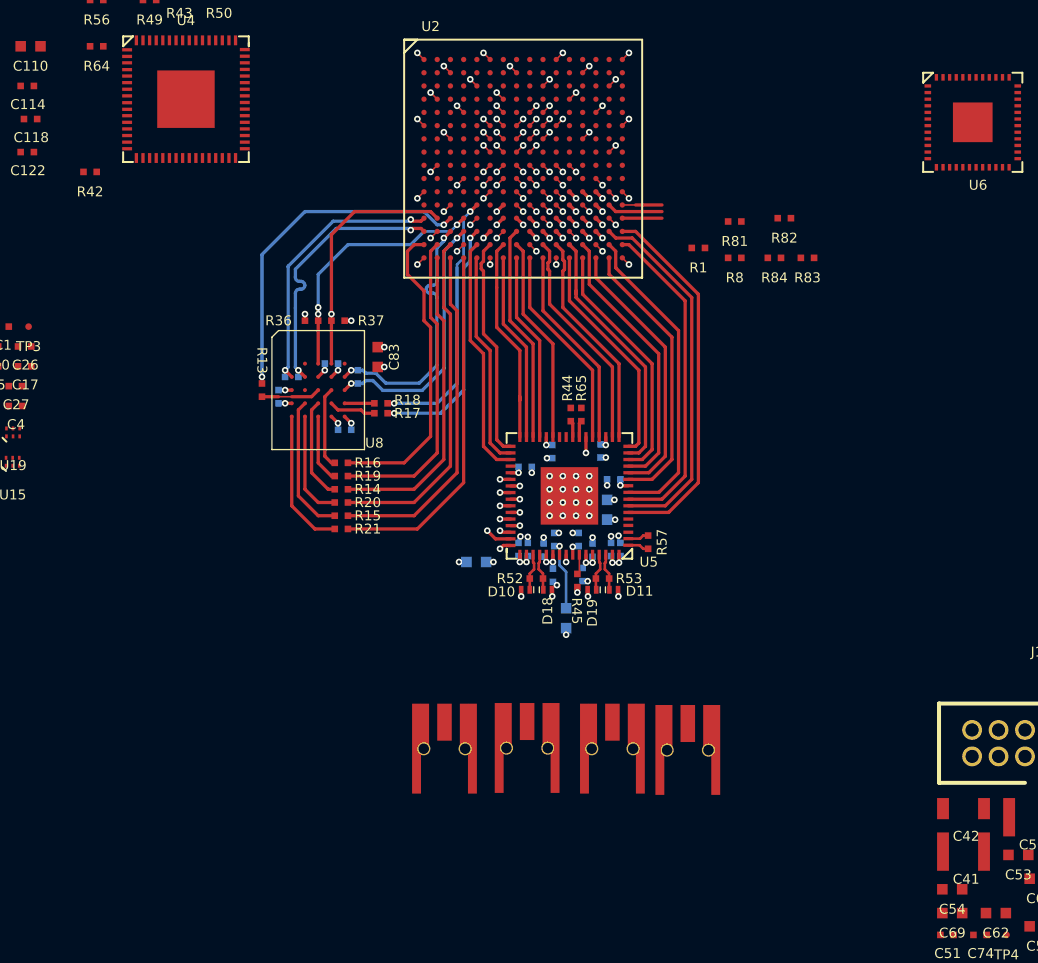
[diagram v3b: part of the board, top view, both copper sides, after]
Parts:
- removed R58, R59, R60, R61: 100, azonenberg_pcb:EIA_0402_RES_NOSILK
- C111, C119, C123, C127, C131, C138, C139, C146, C147, C154, C155, C162, C163, C192, C205, C209, C84, C85, C86, R34, R35: moved to B.Cu
- locked: renamed from C115; moved to B.Cu
- moved C205 29.2 mm to (87.8, 102.2), turned to -90 degrees
- moved C131 27.6 mm to (81.0, 98.0), turned to 180 degrees
- moved C192 27.0 mm to (88.7, 96.3), turned to 90 degrees
- moved C163 25.3 mm to (86.8, 99.0), turned to 90 degrees
- moved C209 24.7 mm to (86.8, 96.3), turned to 90 degrees
- moved C147 22.9 mm to (84.8, 97.0), turned to -90 degrees
- moved C155 22.8 mm to (89.8, 97.1), turned to -90 degrees
- moved C139 21.8 mm to (86.0, 97.1), turned to -90 degrees
- moved C162 21.4 mm to (84.2, 97.0), turned to 90 degrees
- moved C83 15.9 mm to (73.5, 82.5), turned to 90 degrees
- moved D19 15.8 mm to (89.7, 100.1), turned to 180 degrees
- moved D11 15.7 mm to (91.3, 100.1)
- moved D10 15.7 mm to (84.7, 100.1), turned to 180 degrees
- moved C127 15.6 mm to (84.7, 90.8)
- moved R37 15.5 mm to (70.5, 79.8), turned to 180 degrees
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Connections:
- C128 pad 2: Net-(C128-Pad2) -> /GND
- C129 pad 2: Net-(C129-Pad2) -> /GND
- C130 pad 2: Net-(C130-Pad2) -> /GND
- C131 pad 2: Net-(C131-Pad2) -> /GND
- C132 pad 2: Net-(C128-Pad2) -> /GND
- C133 pad 1: Net-(C128-Pad2) -> /GND
- C134 pad 2: Net-(C129-Pad2) -> /GND
- C135 pad 1: Net-(C129-Pad2) -> /GND
- C136 pad 2: Net-(C130-Pad2) -> /GND
- C137 pad 1: Net-(C130-Pad2) -> /GND
- C138 pad 2: Net-(C131-Pad2) -> /GND
- C139 pad 1: Net-(C131-Pad2) -> /GND
- C140 pad 2: Net-(C128-Pad2) -> /GND
- C141 pad 1: Net-(C128-Pad2) -> /GND
- C142 pad 2: Net-(C129-Pad2) -> /GND
- C143 pad 1: Net-(C129-Pad2) -> /GND
- C144 pad 2: Net-(C130-Pad2) -> /GND
- C145 pad 1: Net-(C130-Pad2) -> /GND
- C146 pad 2: Net-(C131-Pad2) -> /GND
- C147 pad 1: Net-(C131-Pad2) -> /GND
- C148 pad 2: Net-(C128-Pad2) -> /GND
- C149 pad 1: Net-(C128-Pad2) -> /GND
- C150 pad 2: Net-(C129-Pad2) -> /GND
- C151 pad 1: Net-(C129-Pad2) -> /GND
- C152 pad 2: Net-(C130-Pad2) -> /GND
- C153 pad 1: Net-(C130-Pad2) -> /GND
- C154 pad 2: Net-(C131-Pad2) -> /GND
- C155 pad 1: Net-(C131-Pad2) -> /GND
- C156 pad 2: Net-(C128-Pad2) -> /GND
- C157 pad 1: Net-(C128-Pad2) -> /GND
- C158 pad 2: Net-(C129-Pad2) -> /GND
- C159 pad 1: Net-(C129-Pad2) -> /GND
- C160 pad 2: Net-(C130-Pad2) -> /GND
- C161 pad 1: Net-(C130-Pad2) -> /GND
- C162 pad 2: Net-(C131-Pad2) -> /GND
- C163 pad 1: Net-(C131-Pad2) -> /GND
- U2 pad M6: /ADCs/D6_1 -> /ADCs/D6_10
- U2 pad N1: /RAM/RAM_DQ0 -> /RAM/RAM_CLK_N
- U2 pad N11: /ADCs/ADCCLK_7 -> /ADCs/ADCCLK_6
- U2 pad N12: /ADCs/D7_4 -> /ADCs/ADC2_OE_N
- U2 pad N13: /ADCs/ADCCLK_6 -> /ADCs/ADCCLK_7
- U2 pad N4: /RAM/RAM_DQ5 -> /RAM/RAM_CS_N
- U2 pad N6: /ADCs/D6_2 -> /ADCs/D6_11
- U2 pad N9: /ADCs/D7_13 -> /ADCs/D6_9
- U2 pad P1: /RAM/RAM_DQ1 -> /RAM/RAM_CLK_P
- U2 pad P10: /ADCs/D7_5 -> /ADCs/ADC1_OE_N
- U2 pad P11: /ADCs/D7_6 -> /ADCs/D6_8
- U2 pad P13: /ADCs/D7_3 -> /ADCs/ADC3_OE_N
- U2 pad P15: /ADCs/ADC1_OE_N -> /ADCs/D7_1
- U2 pad P16: /ADCs/ADC2_OE_N -> /ADCs/D7_0
- U2 pad P3: /RAM/RAM_DQ3 -> /RAM/RAM_PSC_P
- U2 pad P4: /RAM/RAM_DQ2 -> /RAM/RAM_PSC_N
- U2 pad P5: /RAM/RAM_CS_N -> /RAM/RAM_DQ3
- U2 pad P8: /ADCs/D6_3 -> /ADCs/D6_2
- U2 pad P9: /ADCs/D6_0 -> /ADCs/D6_12
- U2 pad R1: /RAM/RAM_DQ7 -> /RAM/RAM_DQ2
- U2 pad R11: /ADCs/D7_12 -> /ADCs/D7_10
- U2 pad R12: /ADCs/D7_7 -> /ADCs/D7_8
- U2 pad R13: /ADCs/D7_9 -> /ADCs/D7_6
- U2 pad R15: /ADCs/ADC3_OE_N -> /ADCs/D7_3
- U2 pad R16: /ADCs/D7_0 -> /ADCs/D7_2
- U2 pad R2: /RAM/RAM_DQ6 -> /RAM/RAM_DQ5
- U2 pad R3: /RAM/RAM_CLK_P -> /RAM/RAM_DQ6
- U2 pad R5: /ADCs/D6_9 -> /ADCs/D6_7
- U2 pad R6: /ADCs/D6_11 -> /ADCs/D6_5
- U2 pad R7: /ADCs/D6_12 -> /ADCs/D6_4
- U2 pad R8: /ADCs/D6_4 -> /ADCs/D6_0
- U2 pad T10: /ADCs/D6_8 -> /ADCs/D7_12
- U2 pad T12: /ADCs/D7_8 -> /ADCs/D7_9
- U2 pad T13: /ADCs/D7_10 -> /ADCs/D7_7
- U2 pad T14: /ADCs/D7_1 -> /ADCs/D7_5
- U2 pad T15: /ADCs/D7_2 -> /ADCs/D7_4
- U2 pad T2: /RAM/RAM_CLK_N -> /RAM/RAM_DQ0
- U2 pad T3: /RAM/RAM_PSC_N -> /RAM/RAM_DQ1
- U2 pad T4: /RAM/RAM_PSC_P -> /RAM/RAM_DQ7
- U2 pad T5: /ADCs/D6_10 -> /ADCs/D6_6
- U2 pad T7: /ADCs/D6_5 -> /ADCs/D6_3
- U2 pad T8: /ADCs/D6_6 -> /ADCs/D6_1
- U2 pad T9: /ADCs/D6_7 -> /ADCs/D7_13
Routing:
- net /GND: track 161.8 -> 297.8 mm, vias 40 -> 83
- net /D1V8: track 117.8 -> 187.3 mm, vias 30 -> 40
- net /ADCs/D7_0: track 0.00 -> 28.2 mm
- net /ADCs/D7_1: track 0.00 -> 27.7 mm
- net /RAM/RAM_DQ7: track 0.00 -> 27.2 mm
- net /RAM/RAM_DQ6: track 0.00 -> 26.1 mm
- net /RAM/RAM_DQ1: track 0.00 -> 26.1 mm
- net /RAM/RAM_DQS: track 0.00 -> 26.0 mm, vias 0 -> 2
- net /ADCs/D7_2: track 0.00 -> 24.8 mm
- net /ADCs/D7_3: track 0.00 -> 23.8 mm
- net /RAM/RAM_DQ5: track 0.00 -> 23.6 mm
- net /RAM/RAM_DQ0: track 0.00 -> 23.6 mm
- net /RAM/RAM_DQ2: track 0.00 -> 23.3 mm
- net /ADCs/D7_4: track 0.00 -> 21.1 mm
- net /RAM/RAM_CLK_N: track 0.00 -> 21.0 mm, vias 0 -> 2
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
